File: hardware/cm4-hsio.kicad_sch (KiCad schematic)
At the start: 3 parts, among them J1 DF40C-100DP-0.4V_51_

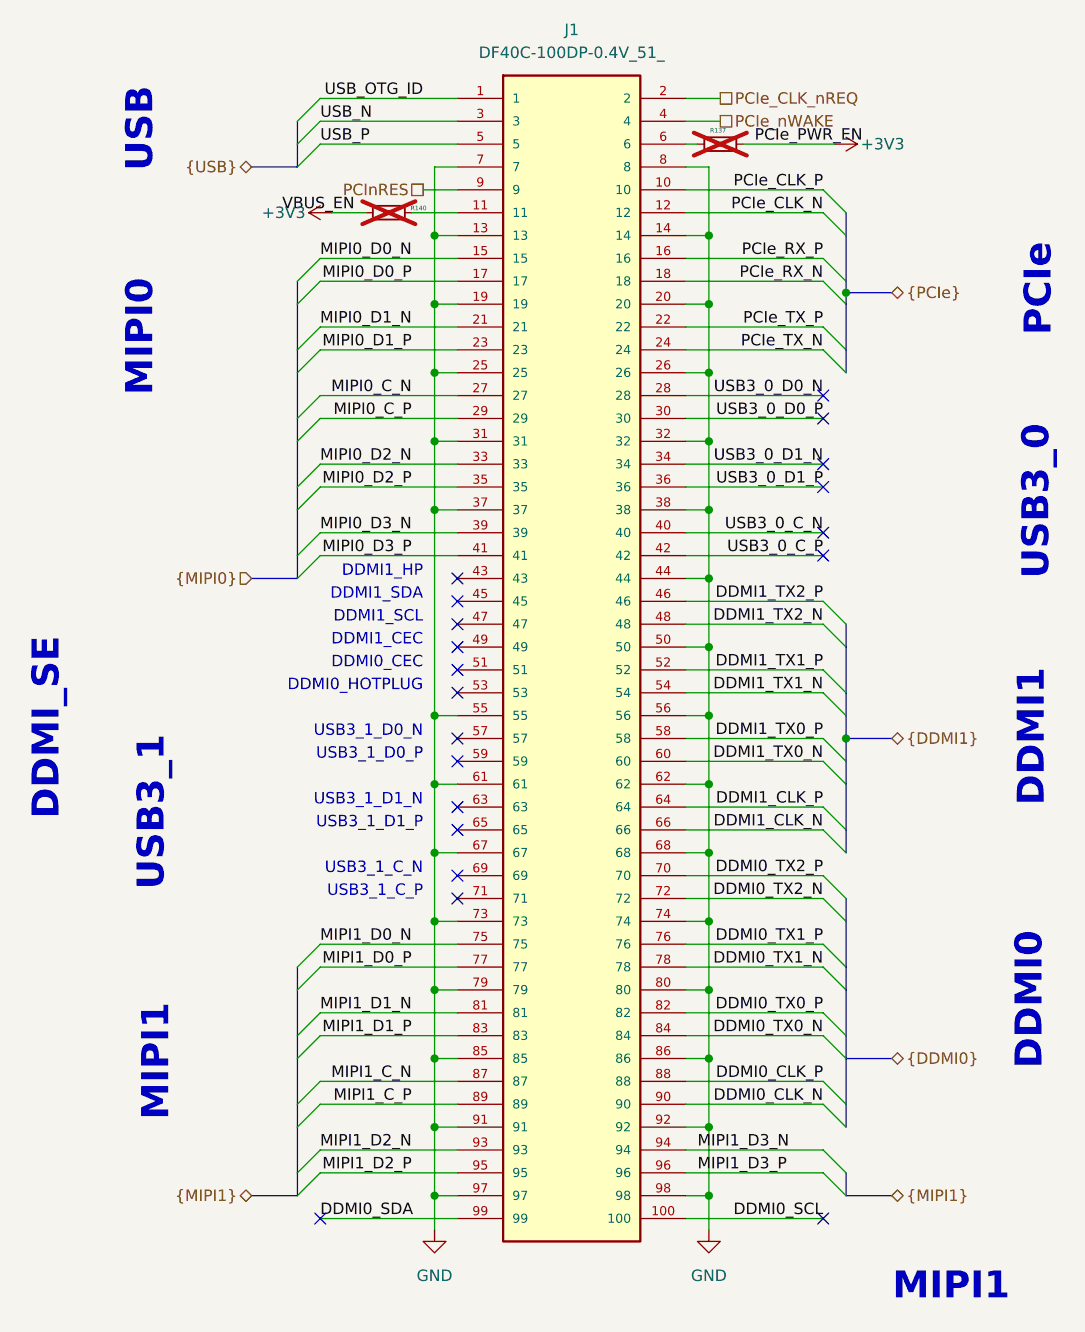
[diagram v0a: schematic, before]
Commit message: Updating sch - moving power select resistors to bottom
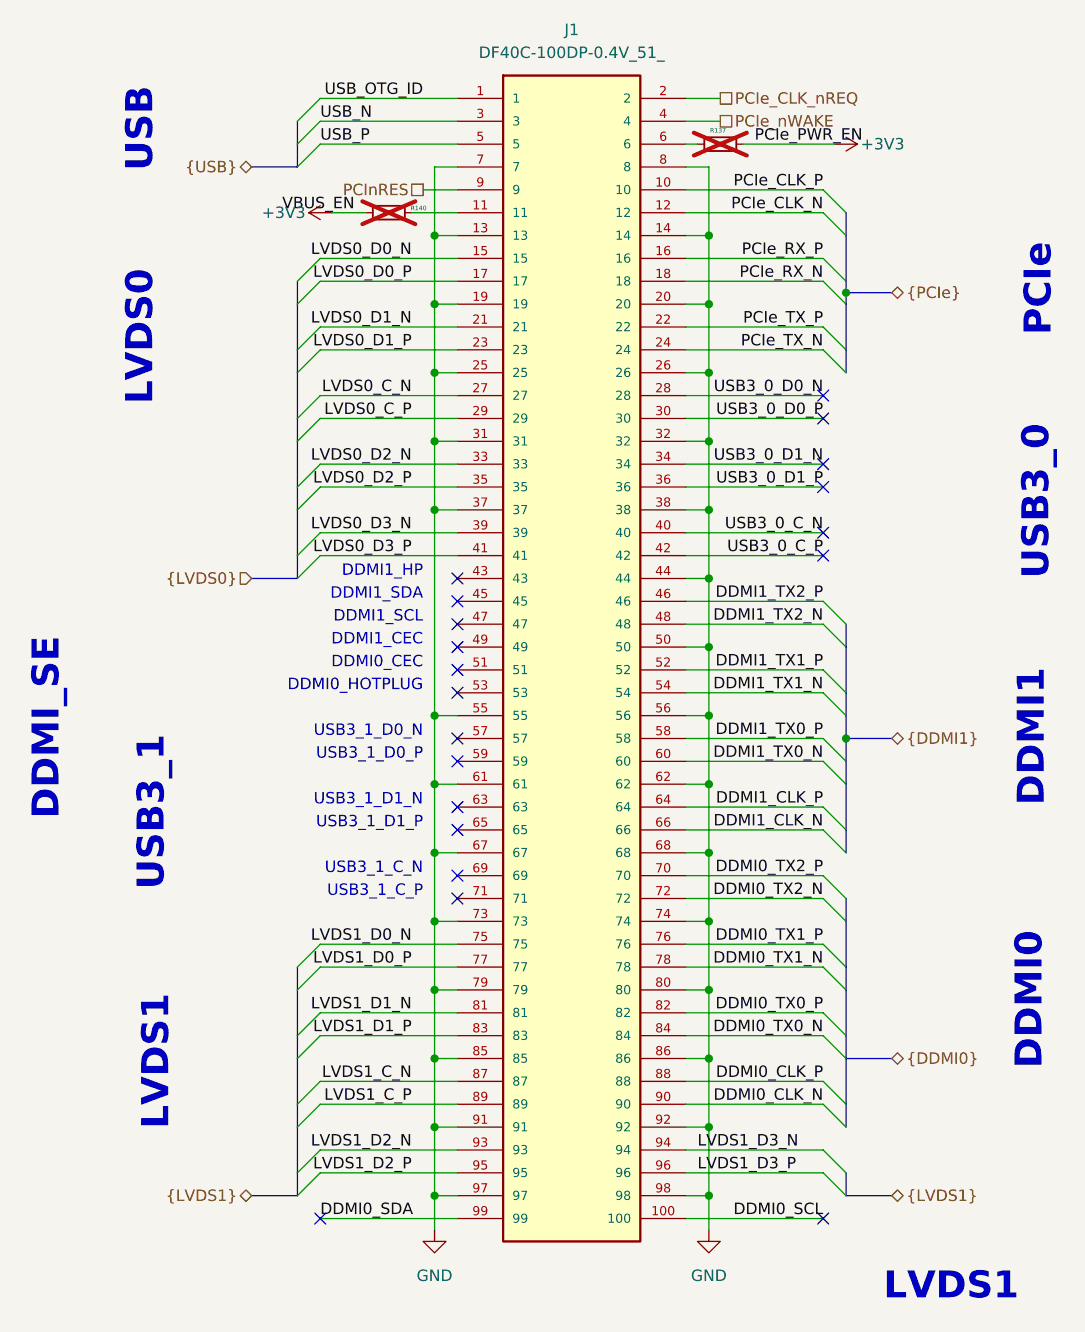
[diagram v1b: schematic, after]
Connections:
- net MIPI0_C_N renamed LVDS0_C_N
- net MIPI0_C_P renamed LVDS0_C_P
- net MIPI0_D0_N renamed LVDS0_D0_N
- net MIPI0_D0_P renamed LVDS0_D0_P
- net MIPI0_D1_N renamed LVDS0_D1_N
- net MIPI0_D1_P renamed LVDS0_D1_P
- net MIPI0_D2_N renamed LVDS0_D2_N
- net MIPI0_D2_P renamed LVDS0_D2_P
- net MIPI0_D3_N renamed LVDS0_D3_N
- net MIPI0_D3_P renamed LVDS0_D3_P
- net MIPI1_C_N renamed LVDS1_C_N
- net MIPI1_C_P renamed LVDS1_C_P
- net MIPI1_D0_N renamed LVDS1_D0_N
- net MIPI1_D0_P renamed LVDS1_D0_P
- net MIPI1_D1_N renamed LVDS1_D1_N
- net MIPI1_D1_P renamed LVDS1_D1_P
- net MIPI1_D2_N renamed LVDS1_D2_N
- net MIPI1_D2_P renamed LVDS1_D2_P
- net MIPI1_D3_N renamed LVDS1_D3_N
- net MIPI1_D3_P renamed LVDS1_D3_P
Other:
- note added: "LVDS0"
- note added: "LVDS1"
- note removed: "MIPI0"
- note removed: "MIPI1"
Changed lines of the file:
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@@
 		(comment 1 "${project_license}")
 	)
-	(bus_alias "MIPI0"
-		(members "MIPI0_D0_P" "MIPI0_D0_N" "MIPI0_D1_P" "MIPI0_D1_N" "MIPI0_D2_P"
-			"MIPI0_D2_N" "MIPI0_C_P" "MIPI0_C_N" "MIPI0_D3_P" "MIPI0_D3_N"
-		)
-	)
-	(bus_alias "MIPI1"
-		(members "MIPI1_D0_P" "MIPI1_D0_N" "MIPI1_D1_P" "MIPI1_D1_N" "MIPI1_D2_P"
-			"MIPI1_D2_N" "MIPI1_D3_P" "MIPI1_D3_N" "MIPI1_C_P" "MIPI1_C_N"
+	(bus_alias "LVDS0"
+		(members "LVDS0_D0_P" "LVDS0_D0_N" "LVDS0_D1_P" "LVDS0_D1_N" "LVDS0_D2_P"
+			"LVDS0_D2_N" "LVDS0_C_P" "LVDS0_C_N" "LVDS0_D3_P" "LVDS0_D3_N"
+		)
+	)
+	(bus_alias "LVDS1"
+		(members "LVDS1_D0_P" "LVDS1_D0_N" "LVDS1_D1_P" "LVDS1_D1_N" "LVDS1_D2_P"
+			"LVDS1_D2_N" "LVDS1_D3_P" "LVDS1_D3_N" "LVDS1_C_P" "LVDS1_C_N"
 		)
 	)
@@
 		)
 	)
-	(text "MIPI0"
+	(text "LVDS0"
 		(exclude_from_sim no)
 		(at 26.924 54.61 90)
@@
 		)
 	)
-	(text "MIPI1"
+	(text "LVDS1"
 		(exclude_from_sim no)
 		(at 28.702 135.128 90)
@@
 		)
 	)
-	(text "MIPI1"
+	(text "LVDS1"
 		(exclude_from_sim no)
 		(at 117.094 160.02 0)
@@
 		)
 	)
-	(label "MIPI1_D1_P"
+	(label "LVDS1_D1_P"
 		(at 57.15 132.08 180)
 		(effects
@@
 		)
 	)
-	(label "MIPI0_D0_N"
+	(label "LVDS0_D0_N"
 		(at 57.15 45.72 180)
 		(effects
@@
 		)
 	)
-	(label "MIPI1_D3_N"
+	(label "LVDS1_D3_N"
 		(at 88.9 144.78 0)
 		(effects
@@
 		)
 	)
-	(label "MIPI1_D3_P"
+	(label "LVDS1_D3_P"
 		(at 88.9 147.32 0)
 		(effects
@@
 		)
 	)
-	(label "MIPI0_D2_P"
+	(label "LVDS0_D2_P"
 		(at 57.15 71.12 180)
 		(effects
@@
 		)
 	)
-	(label "MIPI0_D3_P"
+	(label "LVDS0_D3_P"
 		(at 57.15 78.74 180)
 		(effects
@@
 		)
 	)
-	(label "MIPI1_C_P"
+	(label "LVDS1_C_P"
 		(at 57.15 139.7 180)
 		(effects
@@
 		)
 	)
-	(label "MIPI0_C_P"
+	(label "LVDS0_C_P"
 		(at 57.15 63.5 180)
 		(effects
@@
 		)
 	)
-	(label "MIPI0_D2_N"
+	(label "LVDS0_D2_N"
 		(at 57.15 68.58 180)
 		(effects
@@
 		)
 	)
-	(label "MIPI0_D0_P"
+	(label "LVDS0_D0_P"
 		(at 57.15 48.26 180)
 		(effects
@@
 		)
 	)
-	(label "MIPI1_D0_P"
+	(label "LVDS1_D0_P"
 		(at 57.15 124.46 180)
 		(effects
@@
 		)
 	)
-	(label "MIPI1_D0_N"
+	(label "LVDS1_D0_N"
 		(at 57.15 121.92 180)
 		(effects
@@
 		)
 	)
-	(label "MIPI0_C_N"
+	(label "LVDS0_C_N"
 		(at 57.15 60.96 180)
 		(effects
@@
 		)
 	)
-	(label "MIPI1_D2_P"
+	(label "LVDS1_D2_P"
 		(at 57.15 147.32 180)
 		(effects
@@
 		)
 	)
-	(label "MIPI0_D1_P"
+	(label "LVDS0_D1_P"
 		(at 57.15 55.88 180)
 		(effects
@@
 		)
 	)
-	(label "MIPI0_D1_N"
+	(label "LVDS0_D1_N"
 		(at 57.15 53.34 180)
 		(effects
@@
 		)
 	)
-	(label "MIPI1_D2_N"
+	(label "LVDS1_D2_N"
 		(at 57.15 144.78 180)
 		(effects
@@
 		)
 	)
-	(label "MIPI1_D1_N"
+	(label "LVDS1_D1_N"
 		(at 57.15 129.54 180)
 		(effects
@@
 		)
 	)
-	(label "MIPI1_C_N"
+	(label "LVDS1_C_N"
 		(at 57.15 137.16 180)
 		(effects
@@
 		)
 	)
-	(label "MIPI0_D3_N"
+	(label "LVDS0_D3_N"
 		(at 57.15 76.2 180)
 		(effects
@@
 		)
 	)
-	(hierarchical_label "{MIPI1}"
+	(hierarchical_label "{LVDS1}"
 		(shape bidirectional)
 		(at 110.49 149.86 0)
@@
 		)
 	)
-	(hierarchical_label "{MIPI1}"
+	(hierarchical_label "{LVDS1}"
 		(shape bidirectional)
 		(at 39.37 149.86 180)
@@
 		)
 	)
-	(hierarchical_label "{MIPI0}"
+	(hierarchical_label "{LVDS0}"
 		(shape input)
 		(at 39.37 81.28 180)

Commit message: Tuning LVDS0, LVDS1, DDMIO
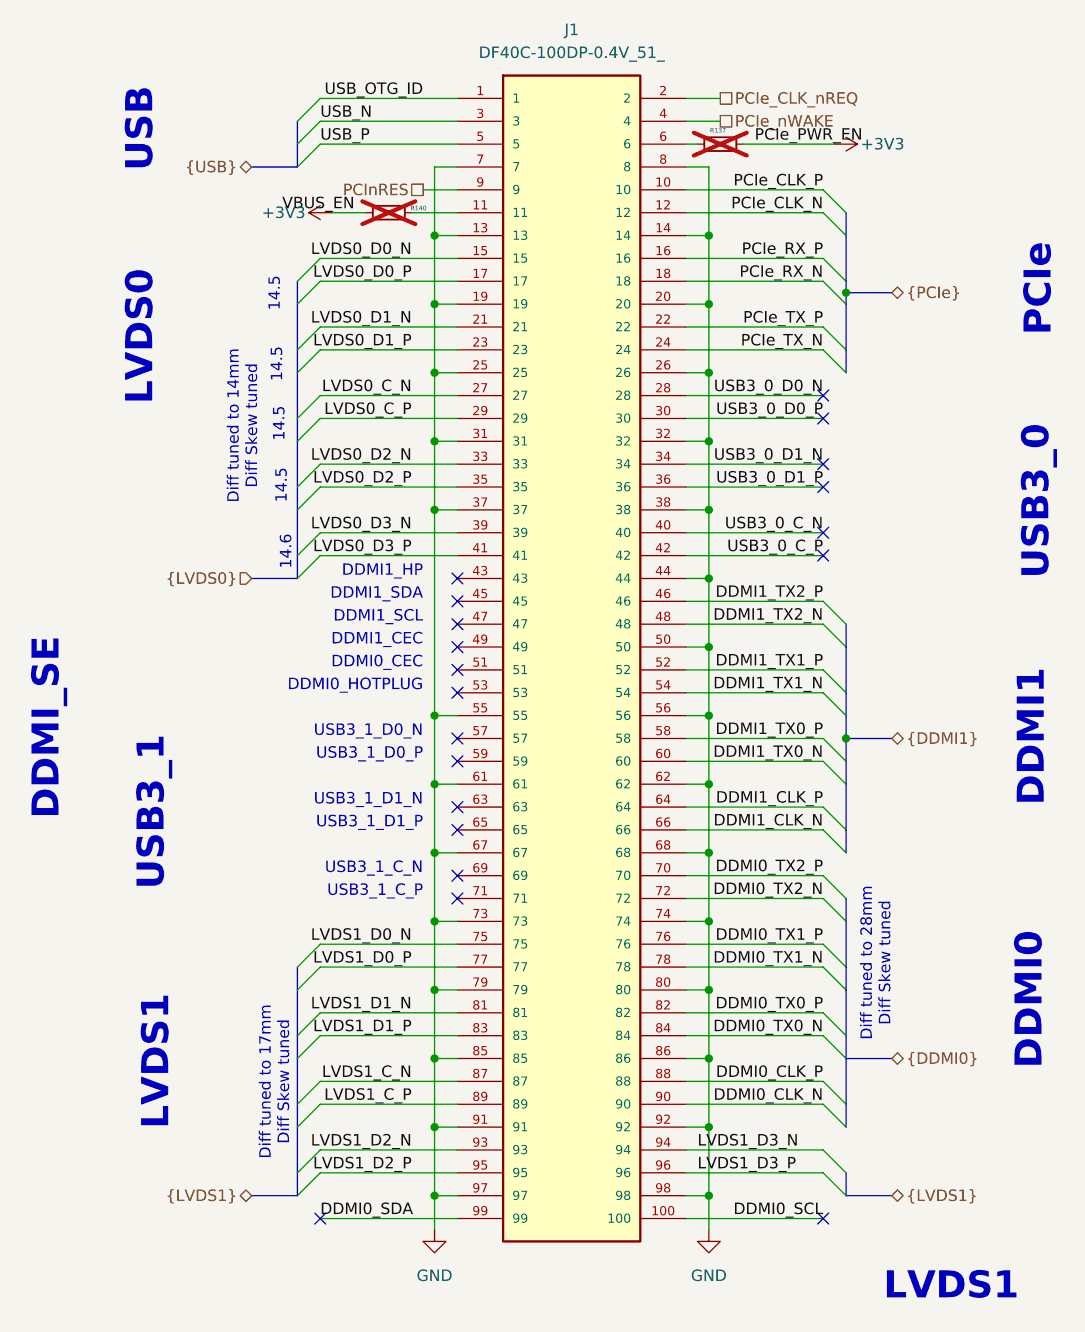
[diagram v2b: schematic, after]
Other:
- note added: "14.5"
- note added: "14.6"
- note added: "Diff tuned to 14mm Diff Skew tuned"
- note added: "Diff tuned to 17mm Diff Skew tuned"
- note added: "Diff tuned to 28mm Diff Skew tuned"
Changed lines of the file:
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@@
+		)
+	)
+	(text "Diff tuned to 14mm\nDiff Skew tuned\n"
+		(exclude_from_sim no)
+		(at 38.354 64.516 90)
+		(effects
+			(font
+				(size 1.27 1.27)
+			)
+		)
+	)
+	(text "14.6"
+		(exclude_from_sim no)
+		(at 43.18 78.486 90)
+		(effects
+			(font
+				(size 1.27 1.27)
+			)
+		)
+	)
+	(text "14.5"
+		(exclude_from_sim no)
+		(at 42.164 57.658 90)
+		(effects
+			(font
+				(size 1.27 1.27)
+			)
 		)
 	)
@@
 		)
 	)
+	(text "14.5"
+		(exclude_from_sim no)
+		(at 42.672 71.12 90)
+		(effects
+			(font
+				(size 1.27 1.27)
+			)
+		)
+	)
 	(text "DDMI1"
 		(exclude_from_sim no)
@@
 		)
 	)
+	(text "14.5"
+		(exclude_from_sim no)
+		(at 42.418 64.262 90)
+		(effects
+			(font
+				(size 1.27 1.27)
+			)
+		)
+	)
 	(text "USB3_1_D1_P"
 		(exclude_from_sim no)
@@
 		)
 	)
+	(text "14.5"
+		(exclude_from_sim no)
+		(at 41.91 49.784 90)
+		(effects
+			(font
+				(size 1.27 1.27)
+			)
+		)
+	)
+	(text "Diff tuned to 17mm\nDiff Skew tuned\n"
+		(exclude_from_sim no)
+		(at 41.91 137.414 90)
+		(effects
+			(font
+				(size 1.27 1.27)
+			)
+		)
+	)
 	(text "LVDS1"
 		(exclude_from_sim no)
@@
 		)
 	)
+	(text "Diff tuned to 28mm\nDiff Skew tuned\n"
+		(exclude_from_sim no)
+		(at 108.712 124.206 90)
+		(effects
+			(font
+				(size 1.27 1.27)
+			)
+		)
+	)

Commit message: SerDes routing improvements
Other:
- note added: "Diff tuned to 25mm Diff Skew tuned"
- note removed: "14.5"
- note removed: "14.6"
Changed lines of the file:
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@@
 	(text "Diff tuned to 14mm\nDiff Skew tuned\n"
 		(exclude_from_sim no)
-		(at 38.354 64.516 90)
-		(effects
-			(font
-				(size 1.27 1.27)
-			)
-		)
-	)
-	(text "14.6"
+		(at 41.402 65.024 90)
+		(effects
+			(font
+				(size 1.27 1.27)
+			)
+		)
+	)
+	(text "Diff tuned to 25mm\nDiff Skew tuned\n"
 		(exclude_from_sim no)
-		(at 43.18 78.486 90)
-		(effects
-			(font
-				(size 1.27 1.27)
-			)
-		)
-	)
-	(text "14.5"
-		(exclude_from_sim no)
-		(at 42.164 57.658 90)
+		(at 108.966 47.752 90)
 		(effects
 			(font
@@
 		)
 	)
-	(text "14.5"
-		(exclude_from_sim no)
-		(at 42.672 71.12 90)
-		(effects
-			(font
-				(size 1.27 1.27)
-			)
-		)
-	)
 	(text "DDMI1"
 		(exclude_from_sim no)
@@
 				(thickness 0.6)
 				(bold yes)
-			)
-		)
-	)
-	(text "14.5"
-		(exclude_from_sim no)
-		(at 42.418 64.262 90)
-		(effects
-			(font
-				(size 1.27 1.27)
 			)
 		)
@@
 		)
 	)
-	(text "14.5"
-		(exclude_from_sim no)
-		(at 41.91 49.784 90)
-		(effects
-			(font
-				(size 1.27 1.27)
-			)
-		)
-	)
 	(text "Diff tuned to 17mm\nDiff Skew tuned\n"
 		(exclude_from_sim no)
@@
 	)
 	(junction
-		(at 105.41 49.53)
-		(diameter 0)
-		(color 0 0 0 0)
-	)
-	(junction
 		(at 90.17 58.42)
 		(diameter 0)
@@
 	(bus
 		(pts
-			(xy 105.41 49.53) (xy 110.49 49.53)
+			(xy 105.41 58.42) (xy 110.49 58.42)
 		)
 		(stroke
@@
 		)
 	)
+	(bus
+		(pts
+			(xy 105.41 48.26) (xy 105.41 50.8)
+		)
+		(stroke
+			(width 0)
+			(type default)
+		)
+	)
 	(wire
 		(pts
@@
 		)
 	)
-	(bus
-		(pts
-			(xy 105.41 55.88) (xy 105.41 58.42)
-		)
-		(stroke
-			(width 0)
-			(type default)
-		)
-	)
 	(wire
 		(pts
@@
 		)
 	)
-	(bus
-		(pts
-			(xy 105.41 48.26) (xy 105.41 49.53)
-		)
-		(stroke
-			(width 0)
-			(type default)
-		)
-	)
 	(wire
 		(pts
@@
 	(bus
 		(pts
+			(xy 105.41 58.42) (xy 105.41 55.88)
+		)
+		(stroke
+			(width 0)
+			(type default)
+		)
+	)
+	(bus
+		(pts
 			(xy 44.45 78.74) (xy 44.45 81.28)
 		)
@@
 		(pts
 			(xy 105.41 134.62) (xy 110.49 134.62)
-		)
-		(stroke
-			(width 0)
-			(type default)
-		)
-	)
-	(bus
-		(pts
-			(xy 105.41 49.53) (xy 105.41 50.8)
 		)
 		(stroke
@@
 	(hierarchical_label "{PCIe}"
 		(shape bidirectional)
-		(at 110.49 49.53 0)
-		(effects
-			(font
+		(at 110.49 58.42 0)
+		(effects
+			(font
